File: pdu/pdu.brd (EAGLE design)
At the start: 17.5 x 90 mm, 62 parts, among them IC1 FDN359BN, IC2 FDN359BN, IC3 FDN359BN, J1 S2B-PH-K-S(LF)(SN), J10 S2B-PH-K-S(LF)(SN), J2 S2B-PH-K-S(LF)(SN), J3 S2B-PH-K-S(LF)(SN), J4 S2B-PH-K-S(LF)(SN), J5 S2B-PH-K-S(LF)(SN), J6 S2B-PH-K-S(LF)(SN), J7 S2B-PH-K-S(LF)(SN), J8 S2B-PH-K-S(LF)(SN), J9 S2B-PH-K-S(LF)(SN)

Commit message: prod files
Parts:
- moved C5 0.25 mm to (-5.33, -34.4)
- moved C8 0.25 mm to (5.33, -34.4)
- moved C7 0.25 mm to (3.17, -34.4)
- moved C4 0.25 mm to (-7.49, -34.4)
- moved C9 0.25 mm to (7.49, -34.4)
- moved C6 0.13 mm to (-3.30, -34.4)
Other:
- board text added: "JLCJLCJLCJLC"

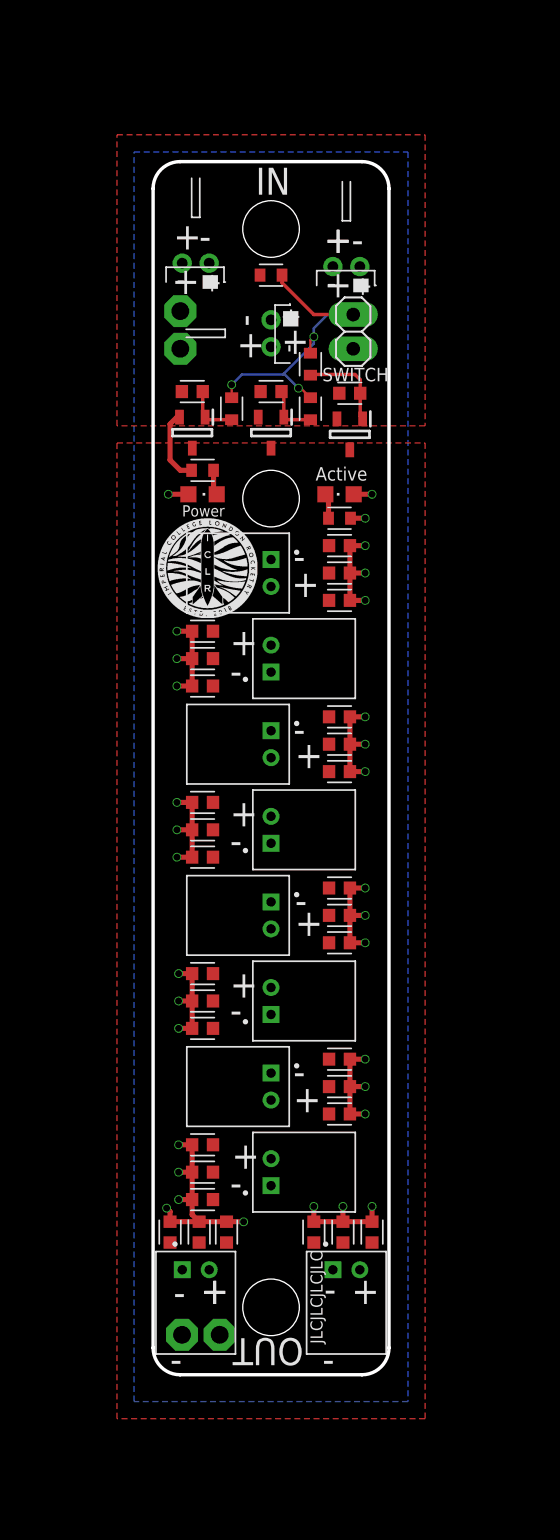
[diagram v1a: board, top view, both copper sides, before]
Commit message: move connectors around for better mech integration
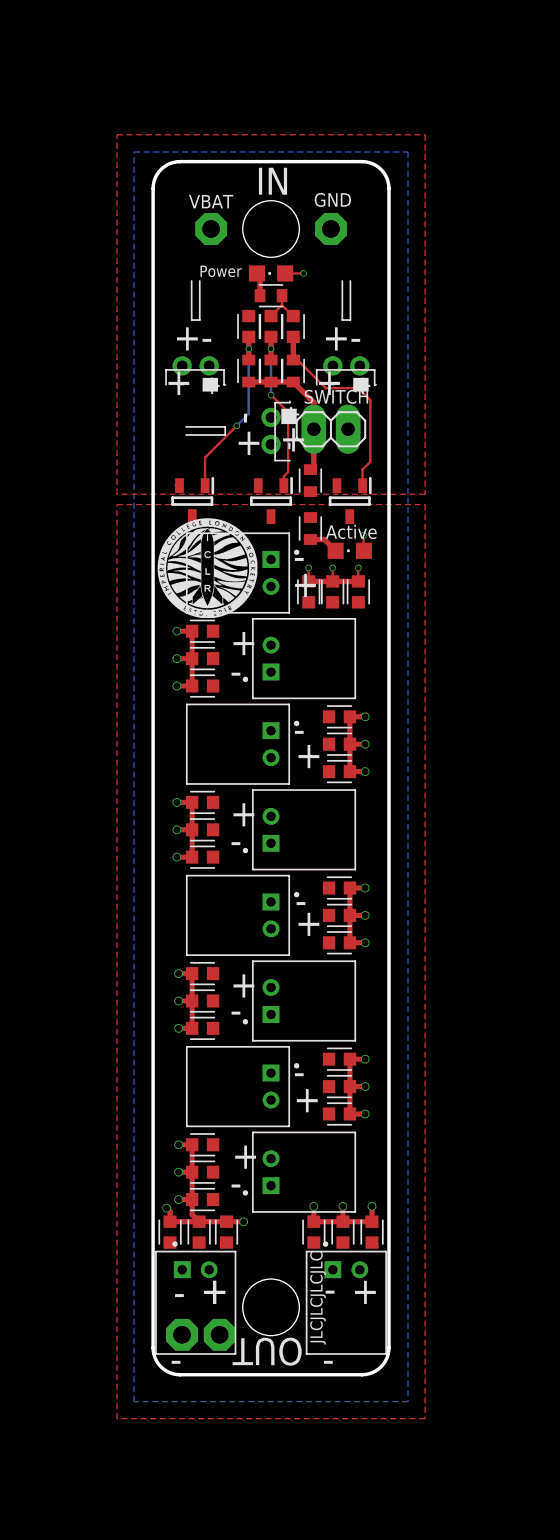
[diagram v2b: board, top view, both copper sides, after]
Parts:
- moved LED3 17.2 mm to (0.00, 36.7), turned to 90 degrees
- moved R2 15.5 mm to (2.92, 21.3), turned to 90 degrees
- moved R6 13.9 mm to (0.00, 35.1), turned to 180 degrees
- moved TP3 12.7 mm to (4.45, 40.0)
- moved TP4 9.18 mm to (-4.45, 40.0)
- moved CN3 7.62 mm to (-5.59, 29.8)
- moved JP1 7.42 mm to (4.45, 25.1), turned to 180 degrees
- moved CN2 7.37 mm to (5.59, 29.8)
- moved CN1 7.24 mm to (0.00, 25.0)
- moved C3 6.49 mm to (1.65, 32.8), turned to 270 degrees
- moved C1 6.39 mm to (-1.65, 32.8), turned to 270 degrees
- moved IC1 5.08 mm to (-5.84, 19.8)
- moved IC2 5.08 mm to (0.00, 19.8)
- moved IC3 4.95 mm to (5.84, 19.8)
- moved C2 4.83 mm to (0.00, 32.8), turned to 270 degrees
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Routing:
- net EN: track 23.7 -> 10.5 mm, vias 3 -> 0
- net N$1: track 4.02 -> 13.7 mm, vias 0 -> 2
- net N$2: track 4.02 -> 12.8 mm, vias 0 -> 2
- net N$3: track 6.85 -> 15.4 mm
- net GND: track 5.49 -> 3.21 mm
- net RET: track 1.09 -> 0.00 mm, vias 1 -> 0
- net VBAT: track 77.9 -> 77.0 mm

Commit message: graphics improvements
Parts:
- moved TP1 11.5 mm to (4.83, -40.8)
- moved TP2 1.80 mm to (-5.08, -40.8)
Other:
- board text added: "Designed by ART Avionics"
- board text added: "Shrey Bohra Shreya Ramteke Sharwa Molla Abhik Chatterjee Camillo De Gregorio"

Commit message: export new pdu
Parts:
- moved C7 9.09 mm to (-5.08, -38.2), turned to 180 degrees
- moved J1 8.00 mm to (5.59, -45.2)
- moved J2 8.00 mm to (-5.59, -45.2)
- moved TP1 7.50 mm to (5.08, -48.3)
- moved TP2 7.49 mm to (-5.08, -48.3)
- moved C4 6.73 mm to (-7.49, -41.1)
- moved C5 6.73 mm to (-5.33, -41.1)
- moved C8 6.73 mm to (5.33, -41.1)
- moved C9 6.73 mm to (7.49, -41.1)
- moved J10 4.53 mm to (0.00, -34.5)
- moved C23 3.89 mm to (4.95, -29.5)
- moved C24 3.89 mm to (4.95, -27.5)
- moved C25 3.89 mm to (4.95, -25.5)
- moved J9 3.88 mm to (0.00, -27.5)
- moved C10 3.87 mm to (-5.08, -31.8)
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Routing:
- net EN: track 10.5 -> 13.3 mm
- net VBAT: track 77.0 -> 74.4 mm, vias 31 -> 32
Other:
- board size 17.5 x 90 mm -> 17.5 x 105 mm
- board text added: ".05"
- board text added: "100"
- board text added: "3.5"
- board text added: "90"
- board text added: "95"
- board text added: "Shrey Bohra Shreya Ramteke Sharwa Molla Hritik Parmessur Abhik Chatterjee Camillo De Gregorio Ella Devesa"
- board text removed: "0.05"
- board text removed: "Shrey Bohra Shreya Ramteke Sharwa Molla Abhik Chatterjee Camillo De Gregorio"

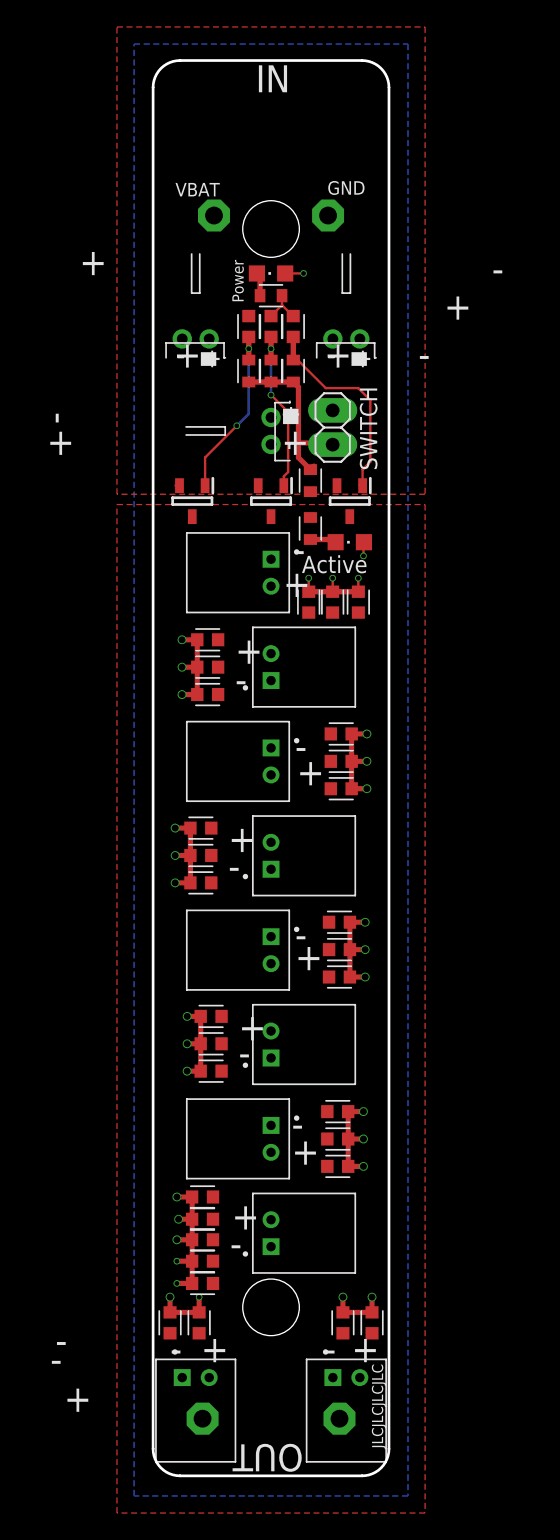
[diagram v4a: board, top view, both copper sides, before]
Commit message: change to single big fet
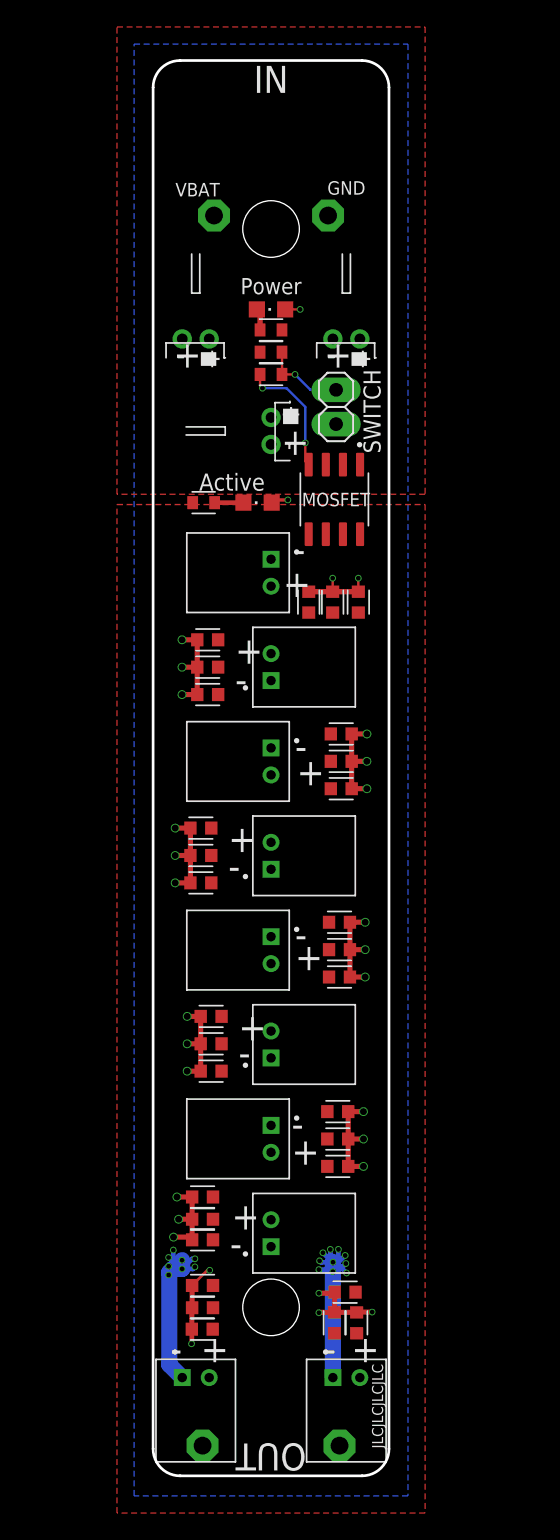
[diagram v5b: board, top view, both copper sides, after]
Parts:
- removed C1, C2, C3: 100p, Capacitor:CAPC1608X85
- removed IC1, IC2, IC3: FDN359BN, SamacSys_Parts:SOT95P251X112-3N
- removed R3, R5: 470, Resistor:RESC1608X60
- added Q1: TSM4806CS_RLG, TSM4806CS_RLG:SOP127P600X200-8N
- moved C4 13.2 mm to (5.50, -38.9), turned to 180 degrees
- moved R2 9.96 mm to (0.00, 30.9), turned to 0 degrees
- moved R4 8.15 mm to (-5.00, 19.7), turned to 180 degrees
- moved LED2 7.45 mm to (-1.00, 19.7)
- moved LED3 2.67 mm to (0.00, 34.0)
- moved R6 2.54 mm to (0.00, 32.5)
- moved TP1 2.00 mm to (5.08, -50.3)
- moved TP2 2.00 mm to (-5.08, -50.3)
- moved C7 1.80 mm to (-5.08, -40.0)
- moved C6 1.80 mm to (-5.08, -38.4)
- moved R1 1.67 mm to (0.00, 29.2), turned to 0 degrees
- moved JP1 1.55 mm to (4.83, 26.8), turned to 90 degrees
- moved C9 1.14 mm to (6.35, -41.1)
- moved C8 0.63 mm to (4.70, -41.1)
- moved C5 0.53 mm to (-5.10, -41.6), turned to 180 degrees
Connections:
- removed net N$2: C2.2, IC2.1, R3.1
- removed net N$3: C3.2, IC3.1, R5.1
- net EN: no longer R3.2, R5.2
- net GND: now also Q1.1, Q1.2, Q1.3; no longer C1.1, C2.1, C3.1, IC1.2, IC2.2, IC3.2
- net N$1: now also Q1.4; no longer C1.2, IC1.1
- net RET: now also Q1.5, Q1.6, Q1.7, Q1.8; no longer IC1.3, IC2.3, IC3.3
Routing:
- net RET: track 0.00 -> 34.6 mm, vias 0 -> 18
- net N$3: track 15.4 -> 0.00 mm
- net N$2: track 12.8 -> 0.00 mm, vias 2 -> 0
- net EN: track 13.3 -> 6.14 mm, vias 0 -> 1
- net N$1: track 13.7 -> 9.23 mm
- net GND: track 3.21 -> 0.00 mm
- net VBAT: track 74.4 -> 72.2 mm, vias 32 -> 30
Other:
- board text added: "MOSFET"

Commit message: final prod versions
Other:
- board text added: "Shrey Bohra Shreya Ramteke Sharwa Molla Hritik Parmessur Abhik Chatterjee Camillo De Gregorio"
- board text removed: "Shrey Bohra Shreya Ramteke Sharwa Molla Hritik Parmessur Abhik Chatterjee Camillo De Gregorio Ella Devesa"
